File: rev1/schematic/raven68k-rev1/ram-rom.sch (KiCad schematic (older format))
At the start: 4 parts

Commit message: update schematic for rev1
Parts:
- added C? (x4): 0.1uF, symbol Device:C
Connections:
- net +5V: now also C?.1, C?.1, C?.1, C?.1
- net GND: now also C?.2, C?.2, C?.2, C?.2
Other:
- note added: "Lower Byte"
- note added: "Upper Byte"
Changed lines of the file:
@@
 $Descr A4 11693 8268
 encoding utf-8
-Sheet 2 4
+Sheet 3 5
 Title ""
 Date ""
@@
 Text HLabel 5900 800  2    50   Input ~ 0
 A[1..23]
-$Comp
-L power:GND #PWR?
-U 1 1 60935735
-P 6550 3500
-F 0 "#PWR?" H 6550 3250 50  0001 C CNN
-F 1 "GND" H 6555 3327 50  0000 C CNN
-F 2 "" H 6550 3500 50  0001 C CNN
-F 3 "" H 6550 3500 50  0001 C CNN
-	1    6550 3500
-	1    0    0    -1
-$EndComp
-$Comp
-L power:GND #PWR?
-U 1 1 60935F1D
-P 6550 6250
-F 0 "#PWR?" H 6550 6000 50  0001 C CNN
-F 1 "GND" H 6555 6077 50  0000 C CNN
-F 2 "" H 6550 6250 50  0001 C CNN
-F 3 "" H 6550 6250 50  0001 C CNN
-	1    6550 6250
-	1    0    0    -1
-$EndComp
-$Comp
-L power:GND #PWR?
-U 1 1 609362BB
-P 2550 6350
-F 0 "#PWR?" H 2550 6100 50  0001 C CNN
-F 1 "GND" H 2555 6177 50  0000 C CNN
-F 2 "" H 2550 6350 50  0001 C CNN
-F 3 "" H 2550 6350 50  0001 C CNN
-	1    2550 6350
-	1    0    0    -1
-$EndComp
-$Comp
-L power:GND #PWR?
-U 1 1 6093681B
-P 2600 3600
-F 0 "#PWR?" H 2600 3350 50  0001 C CNN
-F 1 "GND" H 2605 3427 50  0000 C CNN
-F 2 "" H 2600 3600 50  0001 C CNN
-F 3 "" H 2600 3600 50  0001 C CNN
-	1    2600 3600
-	1    0    0    -1
-$EndComp
 Wire Wire Line
 	2500 3600 2600 3600
@@
 Wire Wire Line
 	2450 6350 2550 6350
-$Comp
-L power:+5V #PWR?
-U 1 1 60951FF9
-P 2950 1400
-F 0 "#PWR?" H 2950 1250 50  0001 C CNN
-F 1 "+5V" H 2965 1573 50  0000 C CNN
-F 2 "" H 2950 1400 50  0001 C CNN
-F 3 "" H 2950 1400 50  0001 C CNN
-	1    2950 1400
-	1    0    0    -1
-$EndComp
-$Comp
-L power:+5V #PWR?
-U 1 1 609528F4
-P 6800 1300
-F 0 "#PWR?" H 6800 1150 50  0001 C CNN
-F 1 "+5V" H 6815 1473 50  0000 C CNN
-F 2 "" H 6800 1300 50  0001 C CNN
-F 3 "" H 6800 1300 50  0001 C CNN
-	1    6800 1300
-	1    0    0    -1
-$EndComp
-$Comp
-L power:+5V #PWR?
-U 1 1 60952D24
-P 6800 4050
-F 0 "#PWR?" H 6800 3900 50  0001 C CNN
-F 1 "+5V" H 6815 4223 50  0000 C CNN
-F 2 "" H 6800 4050 50  0001 C CNN
-F 3 "" H 6800 4050 50  0001 C CNN
-	1    6800 4050
-	1    0    0    -1
-$EndComp
-$Comp
-L power:+5V #PWR?
-U 1 1 60953193
-P 2900 4150
-F 0 "#PWR?" H 2900 4000 50  0001 C CNN
-F 1 "+5V" H 2915 4323 50  0000 C CNN
-F 2 "" H 2900 4150 50  0001 C CNN
-F 3 "" H 2900 4150 50  0001 C CNN
-	1    2900 4150
-	1    0    0    -1
-$EndComp
 Wire Wire Line
 	2900 4150 2450 4150
@@
 Text Label 3000 5050 0    50   ~ 0
 D7
+Wire Wire Line
+	3100 6850 3400 6850
+$Comp
+L Device:C C?
+U 1 1 6201DDC7
+P 3700 7050
+AR Path="/610A1F9D/6201DDC7" Ref="C?"  Part="1"
+AR Path="/60A4B12C/6201DDC7" Ref="C?"  Part="1"
+AR Path="/6077E967/6201DDC7" Ref="C?"  Part="1"
+F 0 "C?" H 3815 7096 50  0000 L CNN
+F 1 "0.1uF" H 3815 7005 50  0000 L CNN
+F 2 "" H 3738 6900 50  0001 C CNN
+F 3 "~" H 3700 7050 50  0001 C CNN
+	1    3700 7050
+	1    0    0    -1
+$EndComp
+Text GLabel 5350 6850 2    50   Output ~ 0
++5V
+Wire Wire Line
+	3100 7300 3400 7300
+Text GLabel 5350 7300 2    50   Output ~ 0
+GND
+$Comp
+L power:GND #PWR?
+U 1 1 6201DDD0
+P 3100 7450
+AR Path="/610A1F9D/6201DDD0" Ref="#PWR?"  Part="1"
+AR Path="/60A4B12C/6201DDD0" Ref="#PWR?"  Part="1"
+F 0 "#PWR?" H 3100 7200 50  0001 C CNN
+F 1 "GND" H 3105 7277 50  0000 C CNN
+F 2 "" H 3100 7450 50  0001 C CNN
+F 3 "" H 3100 7450 50  0001 C CNN
+	1    3100 7450
+	1    0    0    -1
+$EndComp
+$Comp
+L power:+5V #PWR?
+U 1 1 6201DDD6
+P 3100 6700
+AR Path="/610A1F9D/6201DDD6" Ref="#PWR?"  Part="1"
+AR Path="/60A4B12C/6201DDD6" Ref="#PWR?"  Part="1"
+F 0 "#PWR?" H 3100 6550 50  0001 C CNN
+F 1 "+5V" H 3115 6873 50  0000 C CNN
+F 2 "" H 3100 6700 50  0001 C CNN
+F 3 "" H 3100 6700 50  0001 C CNN
+	1    3100 6700
+	1    0    0    -1
+$EndComp
+Wire Wire Line
+	3100 6700 3100 6850
+Wire Wire Line
+	3100 7300 3100 7450
+Connection ~ 3400 6850
+$Comp
+L power:PWR_FLAG #FLG?
+U 1 1 6201DDE0
+P 3400 6850
+AR Path="/610A1F9D/6201DDE0" Ref="#FLG?"  Part="1"
+AR Path="/60A4B12C/6201DDE0" Ref="#FLG?"  Part="1"
+F 0 "#FLG?" H 3400 6925 50  0001 C CNN
+F 1 "PWR_FLAG" H 3400 7023 50  0000 C CNN
+F 2 "" H 3400 6850 50  0001 C CNN
+F 3 "~" H 3400 6850 50  0001 C CNN
+	1    3400 6850
+	1    0    0    -1
+$EndComp
+$Comp
+L power:PWR_FLAG #FLG?
+U 1 1 6201DDE6
+P 3400 7300
+AR Path="/610A1F9D/6201DDE6" Ref="#FLG?"  Part="1"
+AR Path="/60A4B12C/6201DDE6" Ref="#FLG?"  Part="1"
+F 0 "#FLG?" H 3400 7375 50  0001 C CNN
+F 1 "PWR_FLAG" H 3400 7473 50  0000 C CNN
+F 2 "" H 3400 7300 50  0001 C CNN
+F 3 "~" H 3400 7300 50  0001 C CNN
+	1    3400 7300
+	-1   0    0    1
+$EndComp
+Connection ~ 3400 7300
+$Comp
+L Device:C C?
+U 1 1 6202A78C
+P 4150 7050
+AR Path="/610A1F9D/6202A78C" Ref="C?"  Part="1"
+AR Path="/60A4B12C/6202A78C" Ref="C?"  Part="1"
+AR Path="/6077E967/6202A78C" Ref="C?"  Part="1"
+F 0 "C?" H 4265 7096 50  0000 L CNN
+F 1 "0.1uF" H 4265 7005 50  0000 L CNN
+F 2 "" H 4188 6900 50  0001 C CNN
+F 3 "~" H 4150 7050 50  0001 C CNN
+	1    4150 7050
+	1    0    0    -1
+$EndComp
+$Comp
+L Device:C C?
+U 1 1 6202AAEE
+P 4600 7050
+AR Path="/610A1F9D/6202AAEE" Ref="C?"  Part="1"
+AR Path="/60A4B12C/6202AAEE" Ref="C?"  Part="1"
+AR Path="/6077E967/6202AAEE" Ref="C?"  Part="1"
+F 0 "C?" H 4715 7096 50  0000 L CNN
+F 1 "0.1uF" H 4715 7005 50  0000 L CNN
+F 2 "" H 4638 6900 50  0001 C CNN
+F 3 "~" H 4600 7050 50  0001 C CNN
+	1    4600 7050
+	1    0    0    -1
+$EndComp
+$Comp
+L Device:C C?
+U 1 1 6202AE05
+P 5050 7050
+AR Path="/610A1F9D/6202AE05" Ref="C?"  Part="1"
+AR Path="/60A4B12C/6202AE05" Ref="C?"  Part="1"
+AR Path="/6077E967/6202AE05" Ref="C?"  Part="1"
+F 0 "C?" H 5165 7096 50  0000 L CNN
+F 1 "0.1uF" H 5165 7005 50  0000 L CNN
+F 2 "" H 5088 6900 50  0001 C CNN
+F 3 "~" H 5050 7050 50  0001 C CNN
+	1    5050 7050
+	1    0    0    -1
+$EndComp
+Wire Wire Line
+	3400 6850 3700 6850
+Wire Wire Line
+	3700 6900 3700 6850
+Connection ~ 3700 6850
+Wire Wire Line
+	3700 6850 4150 6850
+Wire Wire Line
+	4150 6900 4150 6850
+Connection ~ 4150 6850
+Wire Wire Line
+	4150 6850 4600 6850
+Wire Wire Line
+	3400 7300 3700 7300
+Wire Wire Line
+	5050 6900 5050 6850
+Connection ~ 5050 6850
+Wire Wire Line
+	5050 6850 5350 6850
+Wire Wire Line
+	4600 6900 4600 6850
+Connection ~ 4600 6850
+Wire Wire Line
+	4600 6850 5050 6850
+Wire Wire Line
+	4600 7200 4600 7300
+Connection ~ 4600 7300
+Wire Wire Line
+	4600 7300 5050 7300
+Wire Wire Line
+	5050 7200 5050 7300
+Connection ~ 5050 7300
+Wire Wire Line
+	5050 7300 5350 7300
+Wire Wire Line
+	4150 7200 4150 7300
+Connection ~ 4150 7300
+Wire Wire Line
+	4150 7300 4600 7300
+Wire Wire Line
+	3700 7200 3700 7300
 Wire Bus Line
 	7100 3800 7100 5050
@@
 Wire Bus Line
 	1700 800  1700 6250
+Connection ~ 3700 7300
+Wire Wire Line
+	3700 7300 4150 7300
+Text GLabel 2900 4150 2    50   Input ~ 0
++5V
+Text GLabel 6800 4050 2    50   Input ~ 0
++5V
+Text GLabel 6800 1300 2    50   Input ~ 0
++5V
+Text GLabel 2950 1400 2    50   Input ~ 0
++5V
+Text GLabel 2550 6350 2    50   Input ~ 0
+GND
+Text GLabel 6550 6250 2    50   Input ~ 0
+GND
+Text GLabel 2600 3600 2    50   Input ~ 0
+GND
+Text GLabel 6550 3500 2    50   Input ~ 0
+GND
+Text Notes 4400 1800 0    50   ~ 0
+Upper Byte
+Text Notes 4350 5000 0    50   ~ 0
+Lower Byte
 $EndSCHEMATC

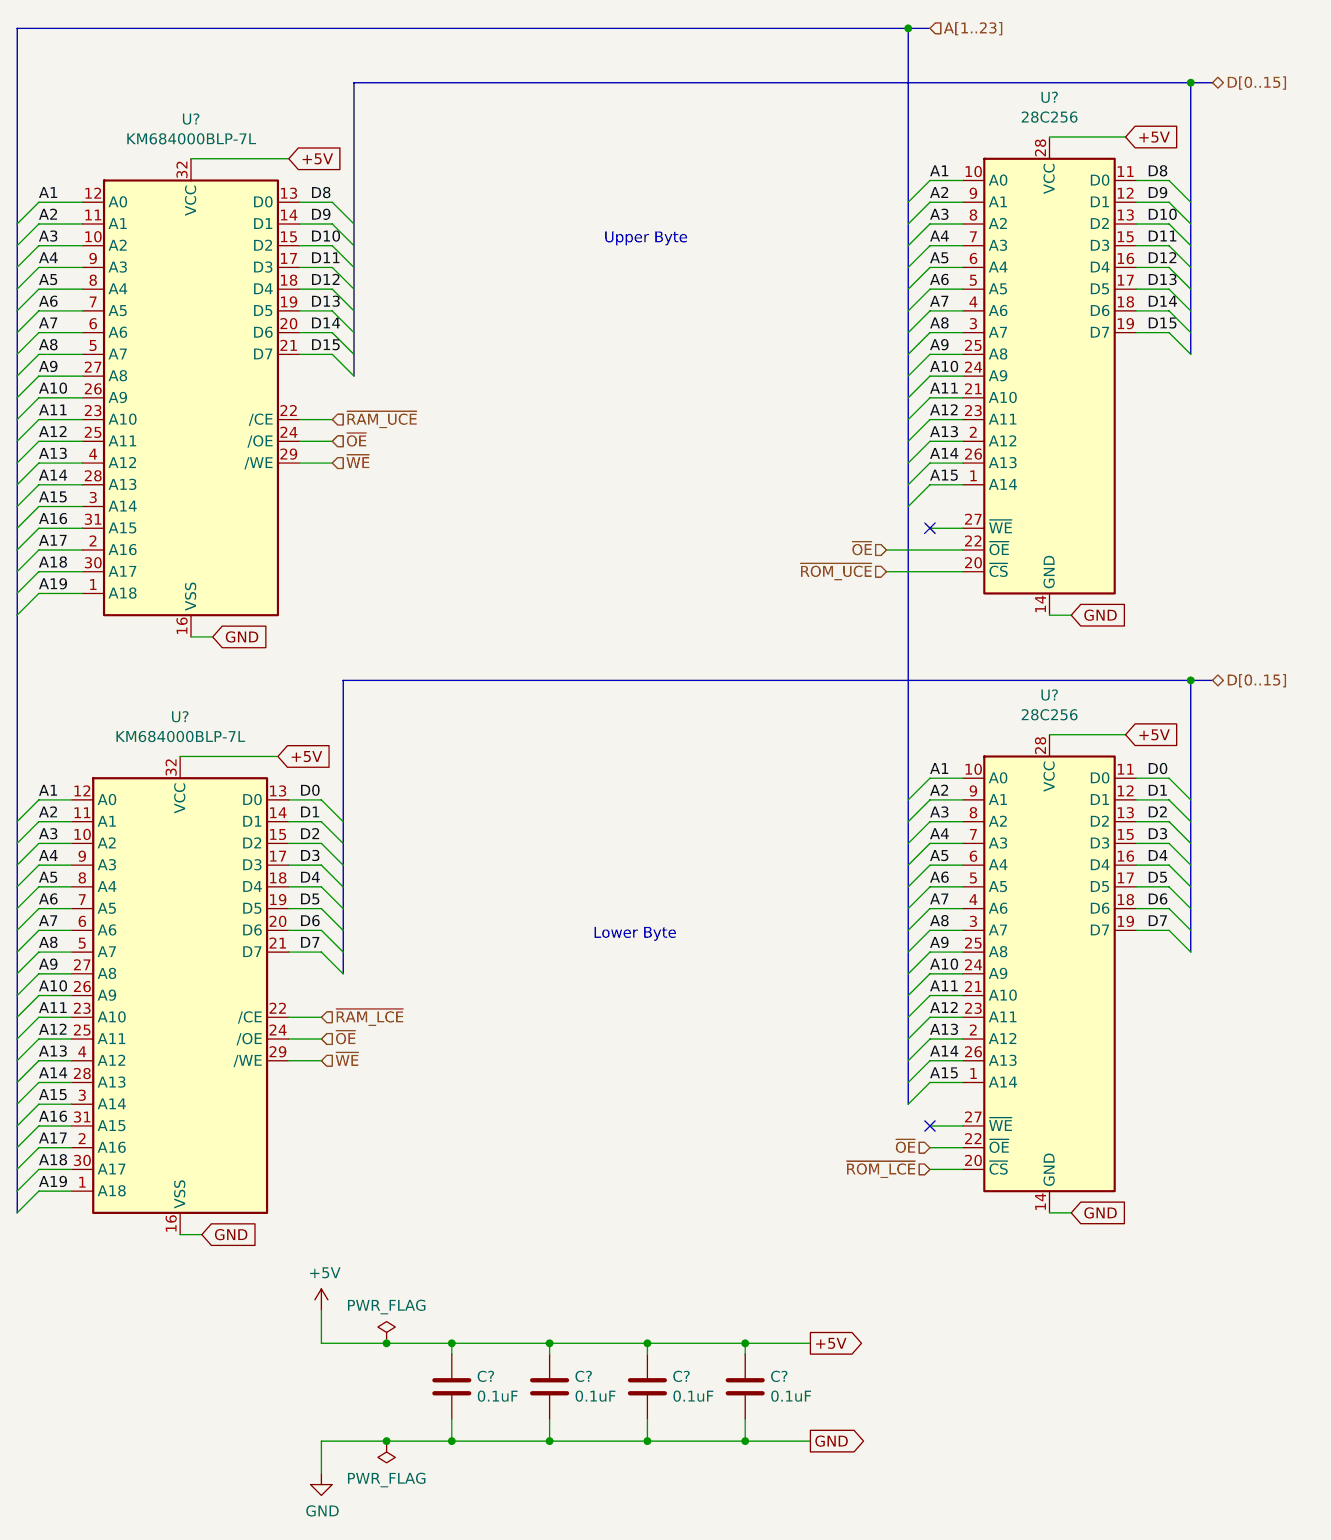
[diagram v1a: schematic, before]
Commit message: added buffers
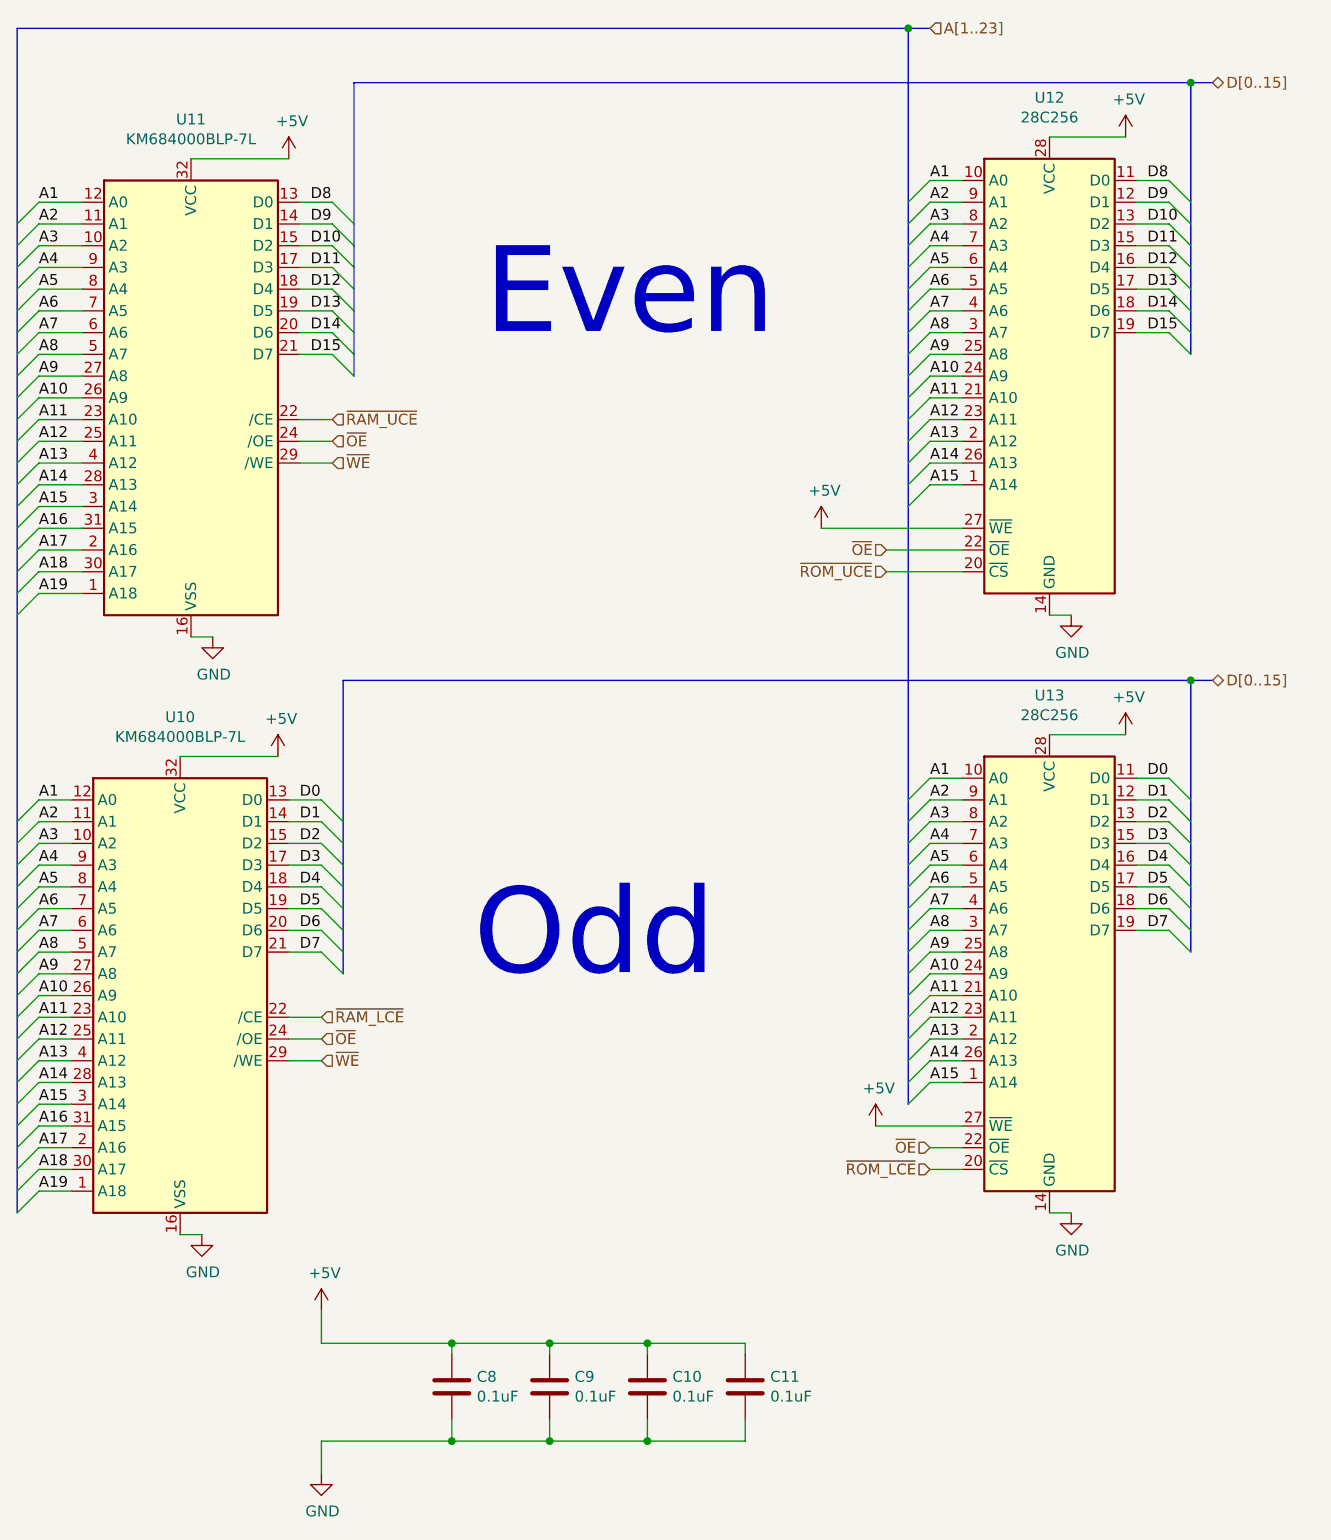
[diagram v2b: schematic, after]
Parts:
- U12, U13: renamed from U?; footprint (none) -> Package_DIP:DIP-28_W7.62mm_Socket
- gave numbers to parts that had none: 6
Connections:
- net +5V: now also U12.27 (~WE), U13.27 (~WE)
- no-connect marks 2 -> 0
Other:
- note added: "Even"
- note added: "Odd"
- note removed: "Lower Byte"
- note removed: "Upper Byte"
